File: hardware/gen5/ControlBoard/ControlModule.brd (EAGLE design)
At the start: 38.5 x 64.9 mm, 44 parts, among them Q1 BSS123, Q2 BSS123, U1 ATMEGA328P-AU

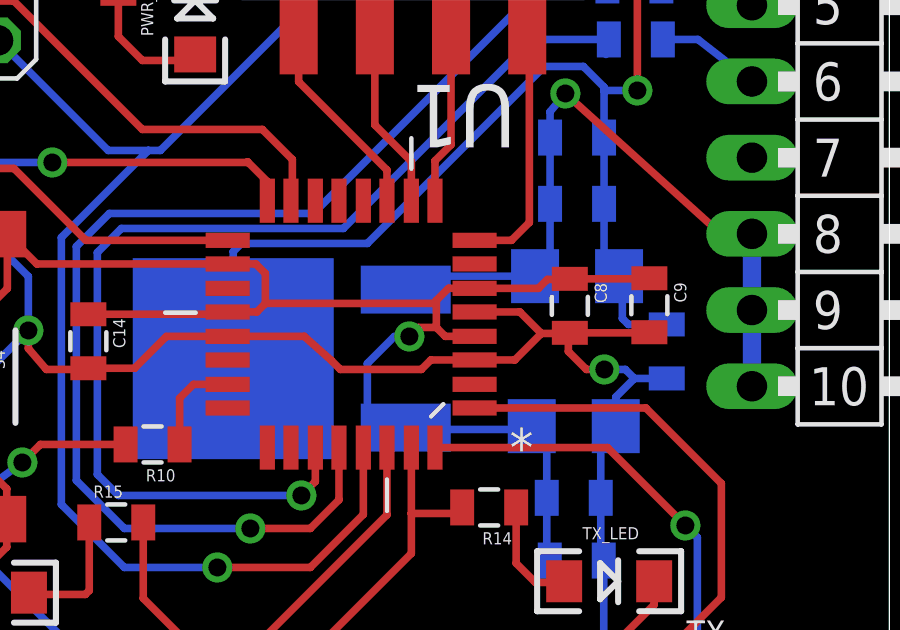
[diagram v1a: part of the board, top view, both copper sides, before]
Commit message: small fix to control module gnd
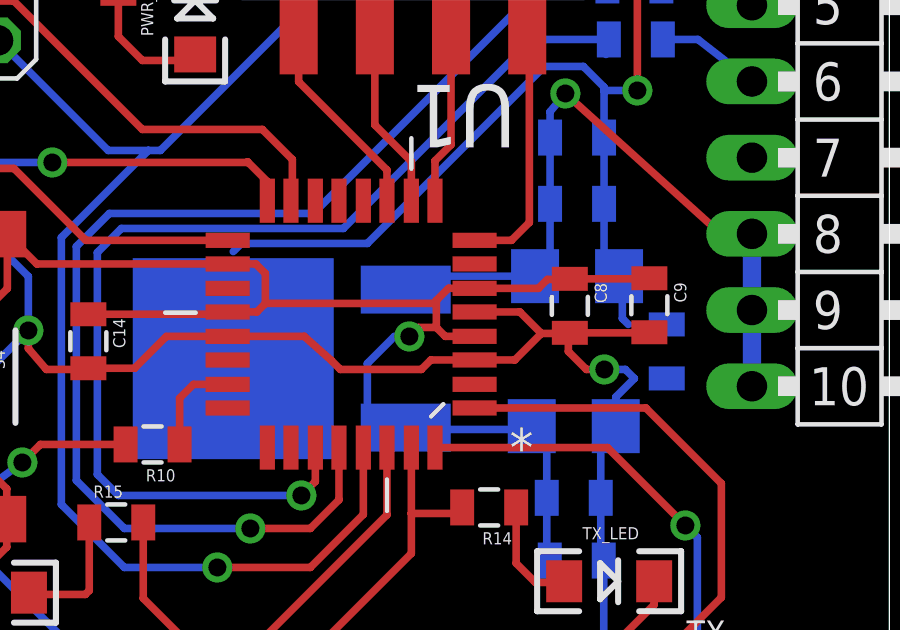
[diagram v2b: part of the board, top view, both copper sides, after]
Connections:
- net 12VGND: no longer 3.3REG.DRAIN
- net GND: now also 3.3REG.DRAIN
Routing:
- net 12VGND: track 44.0 -> 39.1 mm
- net GND: track 155.8 -> 154.8 mm
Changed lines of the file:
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@@
 <?xml version="1.0" encoding="utf-8"?>
 <!DOCTYPE eagle SYSTEM "eagle.dtd">
-<eagle version="7.6.0">
+<eagle version="7.2.0">
 <drawing>
 <settings>
@@
 <contactref element="C7" pad="2"/>
 <contactref element="C10" pad="2"/>
-<contactref element="U$2" pad="2"/>
 <contactref element="U$1" pad="8"/>
 <contactref element="U$1" pad="7"/>
@@
 <wire x1="29.38" y1="39.01" x2="29.38" y2="39.98" width="0.254" layer="16"/>
 <wire x1="29.38" y1="39.98" x2="30" y2="40.6" width="0.254" layer="16"/>
-<wire x1="30" y1="40.6" x2="31.08" y2="40.6" width="0.254" layer="16"/>
 <wire x1="11.68" y1="58.5" x2="14.4" y2="58.5" width="0.254" layer="16"/>
 <wire x1="7.48" y1="53.1" x2="1.2" y2="53.1" width="0.254" layer="16"/>
@@
 <wire x1="9.8" y1="42.2" x2="9.8" y2="44" width="0.254" layer="16"/>
 <wire x1="9.8" y1="44" x2="1.2" y2="52.6" width="0.254" layer="16"/>
+<contactref element="U$2" pad="2"/>
+<contactref element="3.3REG" pad="DRAIN"/>
+<wire x1="30" y1="40.6" x2="31.08" y2="40.6" width="0" layer="19" extent="16-16"/>
+<wire x1="16.63" y1="41.26" x2="16.4416" y2="42" width="0" layer="19" extent="1-16"/>
 </signal>
 <signal name="3.3V">
@@
 </signal>
 <signal name="12VGND">
-<contactref element="U$2" pad="1"/>
 <contactref element="C6" pad="2"/>
-<contactref element="3.3REG" pad="DRAIN"/>
 <contactref element="C4" pad="2"/>
 <contactref element="C5" pad="2"/>
-<wire x1="31.08" y1="42.4" x2="29.8" y2="42.4" width="0.254" layer="16"/>
 <wire x1="29.8" y1="42.4" x2="29.6" y2="42.6" width="0.254" layer="16"/>
 <wire x1="29.6" y1="42.6" x2="29.6" y2="43.9" width="0.254" layer="16"/>
@@
 <wire x1="28.99" y1="46.42" x2="28.99" y2="44.51" width="0.254" layer="16"/>
 <wire x1="28.99" y1="44.51" x2="29.49" y2="44.01" width="0.254" layer="16"/>
-<wire x1="16.63" y1="41.26" x2="16.63" y2="44.83" width="0.254" layer="16"/>
 <wire x1="16.63" y1="44.83" x2="16.9" y2="45.1" width="0.254" layer="16"/>
 <wire x1="16.9" y1="45.1" x2="21.1" y2="45.1" width="0.254" layer="16"/>
@@
 <via x="30.1" y="50.2" extent="1-16" drill="0.6"/>
 <wire x1="30.1" y1="50.2" x2="28.99" y2="50.2" width="0.254" layer="16"/>
+<contactref element="U$2" pad="1"/>
+<wire x1="29.8" y1="42.4" x2="31.08" y2="42.4" width="0" layer="19" extent="16-16"/>
 </signal>
 <signal name="N$4">
